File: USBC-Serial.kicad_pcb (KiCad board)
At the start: 2 copper layers, 19.5 x 25.9 mm, 10 parts, among them J1 USB_C_Receptacle_USB2.0_16P, J2 Conn_01x06_Pin, U1 CH343P

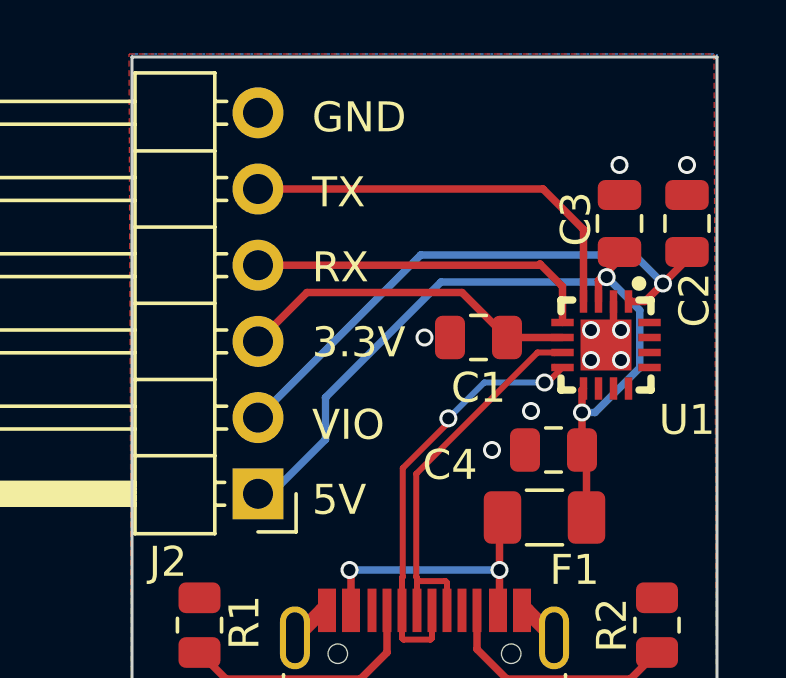
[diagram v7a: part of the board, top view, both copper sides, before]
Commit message: fix bypass caps' ground return path
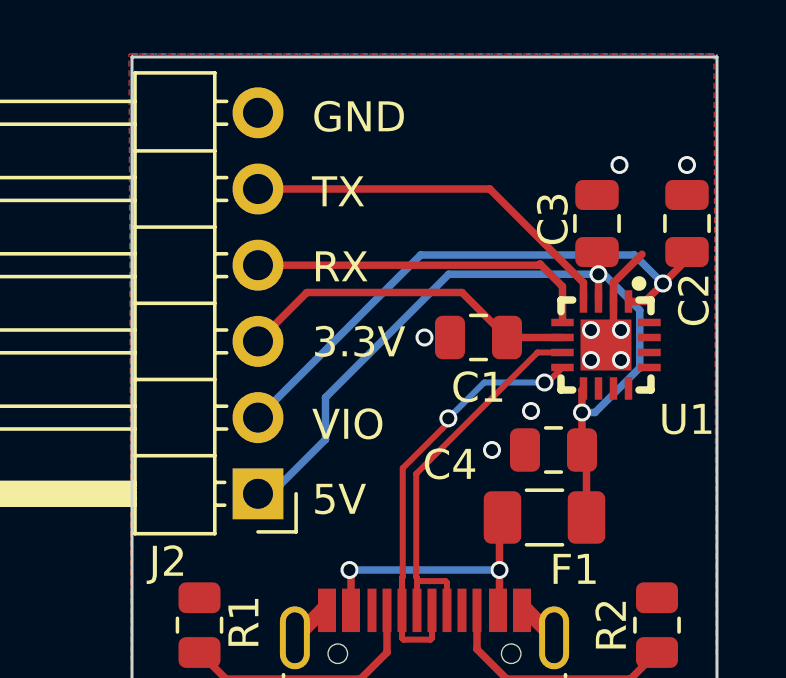
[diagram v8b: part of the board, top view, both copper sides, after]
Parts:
- moved C3 0.75 mm to (28.5, 21.9)
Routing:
- net GND: track 5.09 -> 7.05 mm
- net /TXD: track 13.8 -> 12.8 mm
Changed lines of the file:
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@@
   )
   (footprint "Capacitor_SMD:C_0805_2012Metric" (layer "F.Cu")
-    (at 29.25 21.95 -90)
+    (at 28.5 21.95 -90)
     (descr "Capacitor SMD 0805 (2012 Metric), square (rectangular) end terminal, IPC_7351 nominal, (Body size source: IPC-SM-782 page 76, https://www.pcb-3d.com/wordpress/wp-content/uploads/ipc-sm-782a_amendment_1_and_2.pdf, https://docs.google.com/spreadsheets/d/1BsfQQcO9C6DZCsRaXUlFlo91Tg2WpOkGARC1WS5S8t0/edit?usp=sharing), generated with kicad-footprint-generator")
     (tags "capacitor")
@@
   (segment (start 18.83 24.25) (end 24 24.25) (width 0.25) (layer "F.Cu") (net 1))
   (segment (start 17.2 25.88) (end 18.83 24.25) (width 0.25) (layer "F.Cu") (net 1))
+  (segment (start 29.05 23.925) (end 30 22.975) (width 0.25) (layer "F.Cu") (net 2))
   (segment (start 15.425 34.425) (end 15.25 34.425) (width 0.25) (layer "F.Cu") (net 2))
+  (segment (start 29.05 24.55) (end 29.05 23.925) (width 0.25) (layer "F.Cu") (net 2))
   (segment (start 26.075 34.770483) (end 26 34.845483) (width 0.25) (layer "F.Cu") (net 2))
   (segment (start 26.155 34.845483) (end 27.07 35.760483) (width 0.5) (layer "F.Cu") (net 2))
@@
   (segment (start 29.75 23) (end 30.7 23.95) (width 0.25) (layer "B.Cu") (net 3))
   (segment (start 22.62 23) (end 29.75 23) (width 0.25) (layer "B.Cu") (net 3))
+  (segment (start 28.55 23.75) (end 28.55 22.95) (width 0.25) (layer "F.Cu") (net 4))
   (segment (start 28 29.5) (end 28 28.25) (width 0.25) (layer "F.Cu") (net 4))
   (segment (start 28 28.25) (end 28 27.5) (width 0.25) (layer "F.Cu") (net 4))
-  (segment (start 29.25 23.15) (end 28.55 23.85) (width 0.25) (layer "F.Cu") (net 4))
-  (segment (start 28.663039 23.736961) (end 28.55 23.85) (width 0.25) (layer "F.Cu") (net 4))
+  (segment (start 28.55 24.55) (end 28.55 23.75) (width 0.25) (layer "F.Cu") (net 4))
   (segment (start 28 27.5) (end 28.05 27.45) (width 0.25) (layer "F.Cu") (net 4))
   (segment (start 28.15 31.75) (end 28.15 29.65) (width 0.25) (layer "F.Cu") (net 4))
+  (segment (start 28.55 23.75) (end 28.55 23.642499) (width 0.25) (layer "F.Cu") (net 4))
   (segment (start 28.15 29.65) (end 28 29.5) (width 0.25) (layer "F.Cu") (net 4))
-  (segment (start 28.55 23.85) (end 28.55 24.55) (width 0.25) (layer "F.Cu") (net 4))
-  (segment (start 28.821932 23.736961) (end 28.663039 23.736961) (width 0.25) (layer "F.Cu") (net 4))
-  (via (at 28.821932 23.736961) (size 0.6) (drill 0.4) (layers "F.Cu" "B.Cu") (net 4))
+  (segment (start 28.55 22.95) (end 28.5 22.9) (width 0.25) (layer "F.Cu") (net 4))
+  (segment (start 28.55 23.642499) (end 28.549477 23.641976) (width 0.25) (layer "F.Cu") (net 4))
+  (via (at 28.549477 23.641976) (size 0.6) (drill 0.4) (layers "F.Cu" "B.Cu") (net 4))
   (via (at 28 28.25) (size 0.6) (drill 0.4) (layers "F.Cu" "B.Cu") (net 4))
   (segment (start 29.925 26.758884) (end 28.433884 28.25) (width 0.25) (layer "B.Cu") (net 4))
   (segment (start 29.925 24.840029) (end 29.925 26.758884) (width 0.25) (layer "B.Cu") (net 4))
-  (segment (start 19.45 29.15) (end 19.45 27.75) (width 0.25) (layer "B.Cu") (net 4))
-  (segment (start 23.3 23.9) (end 28.658893 23.9) (width 0.25) (layer "B.Cu") (net 4))
-  (segment (start 17.2 30.96) (end 17.64 30.96) (width 0.25) (layer "B.Cu") (net 4))
-  (segment (start 28.821932 23.736961) (end 29.925 24.840029) (width 0.25) (layer "B.Cu") (net 4))
-  (segment (start 28.658893 23.9) (end 28.821932 23.736961) (width 0.25) (layer "B.Cu") (net 4))
+  (segment (start 23.558024 23.641976) (end 19.45 27.75) (width 0.25) (layer "B.Cu") (net 4))
+  (segment (start 19.45 27.75) (end 19.45 29.15) (width 0.25) (layer "B.Cu") (net 4))
+  (segment (start 28.549477 23.641976) (end 28.726947 23.641976) (width 0.25) (layer "B.Cu") (net 4))
+  (segment (start 28.726947 23.641976) (end 29.925 24.840029) (width 0.25) (layer "B.Cu") (net 4))
   (segment (start 28.433884 28.25) (end 28 28.25) (width 0.25) (layer "B.Cu") (net 4))
-  (segment (start 17.64 30.96) (end 19.45 29.15) (width 0.25) (layer "B.Cu") (net 4))
-  (segment (start 19.45 27.75) (end 23.3 23.9) (width 0.25) (layer "B.Cu") (net 4))
+  (segment (start 19.45 29.15) (end 17.64 30.96) (width 0.25) (layer "B.Cu") (net 4))
+  (segment (start 17.64 30.96) (end 17.2 30.96) (width 0.25) (layer "B.Cu") (net 4))
+  (segment (start 28.549477 23.641976) (end 23.558024 23.641976) (width 0.25) (layer "B.Cu") (net 4))
   (segment (start 25.25 33.5) (end 25.25 34.795483) (width 0.25) (layer "F.Cu") (net 5))
   (segment (start 25.25 31.85) (end 25.35 31.75) (width 0.25) (layer "F.Cu") (net 5))
@@
   (segment (start 27.35 24.05) (end 26.6 23.3) (width 0.25) (layer "F.Cu") (net 12))
   (segment (start 26.6 23.3) (end 26.56 23.34) (width 0.25) (layer "F.Cu") (net 12))
-  (segment (start 28.05 24.55) (end 28.05 22.15) (width 0.25) (layer "F.Cu") (net 13))
-  (segment (start 26.7 20.8) (end 17.2 20.8) (width 0.25) (layer "F.Cu") (net 13))
-  (segment (start 28.05 22.15) (end 26.7 20.8) (width 0.25) (layer "F.Cu") (net 13))
+  (segment (start 28.05 23.925) (end 24.925 20.8) (width 0.25) (layer "F.Cu") (net 13))
+  (segment (start 24.925 20.8) (end 17.2 20.8) (width 0.25) (layer "F.Cu") (net 13))
+  (segment (start 28.05 24.55) (end 28.05 23.925) (width 0.25) (layer "F.Cu") (net 13))
   (zone (net 2) (net_name "GND") (layer "F.Cu") (hatch edge 0.5)
     (connect_pads (clearance 0.5))
